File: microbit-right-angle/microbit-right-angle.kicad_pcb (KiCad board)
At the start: 2 copper layers, 58.9 x 24.4 mm, 2 parts, among them J1 microbit_edge, J2 microbit_smd_socket

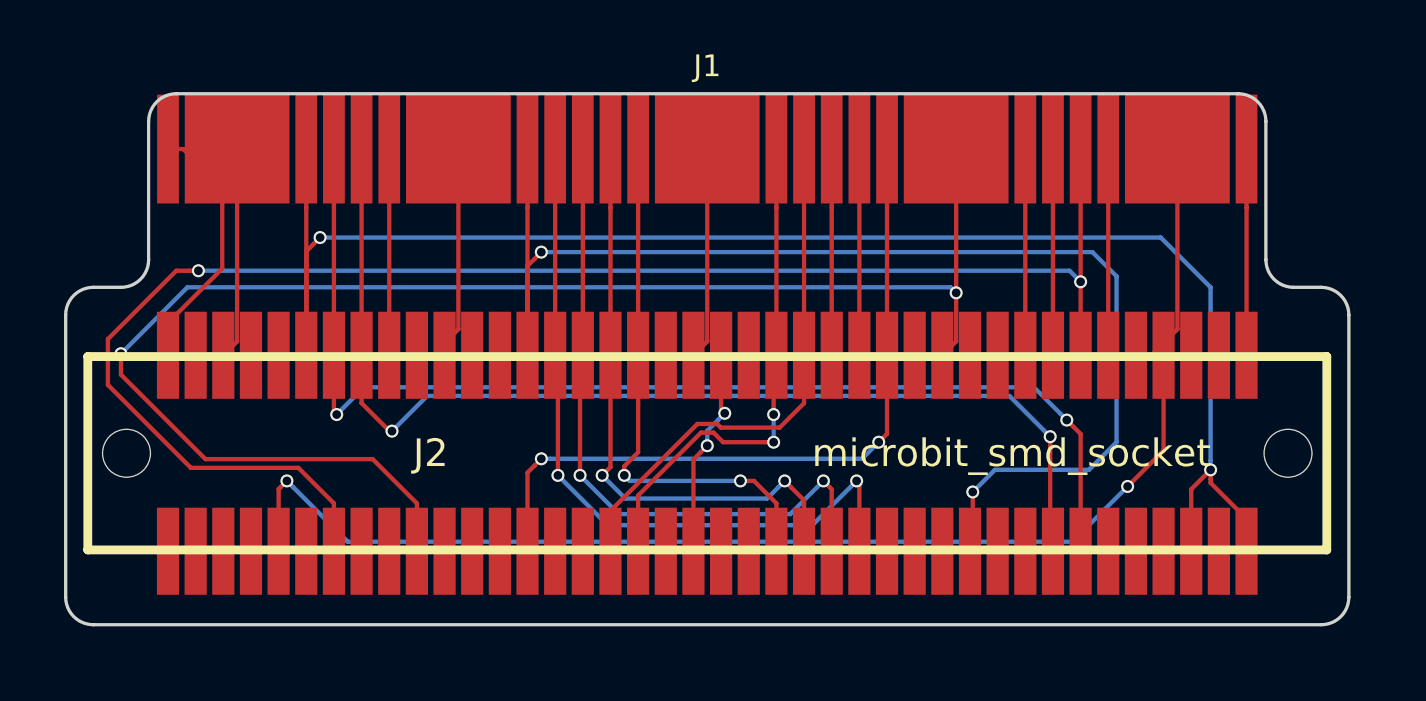
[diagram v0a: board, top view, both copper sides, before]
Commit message: Add ncss/oshw logos and URL
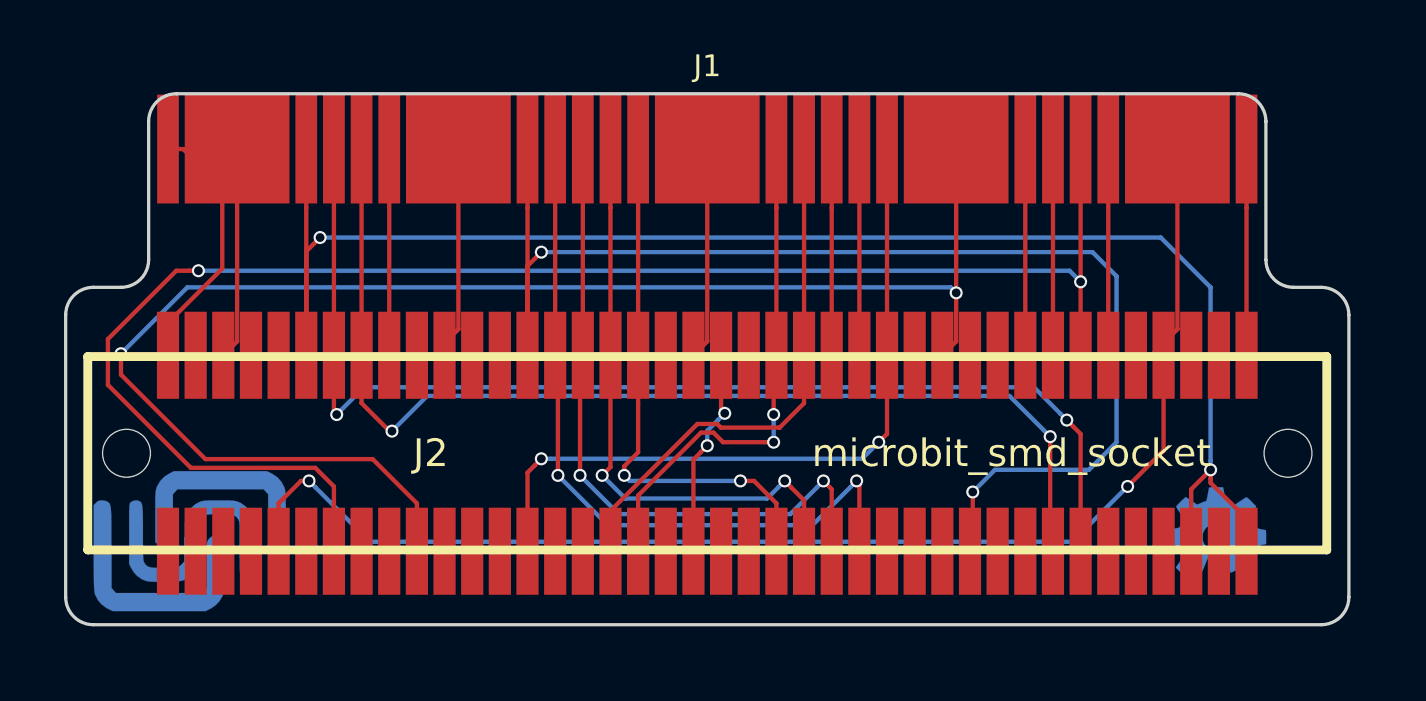
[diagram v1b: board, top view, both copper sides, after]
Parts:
- added Z1: ncss, logos:ncss, B.Cu at (127.3, 108.2)
- added Z2: oshw, logos:OSHW-Logo2_7.3x6mm_Copper, B.Cu at (174.2, 108.2)
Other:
- board text added: "github.com/jimmo/microbit-boards"

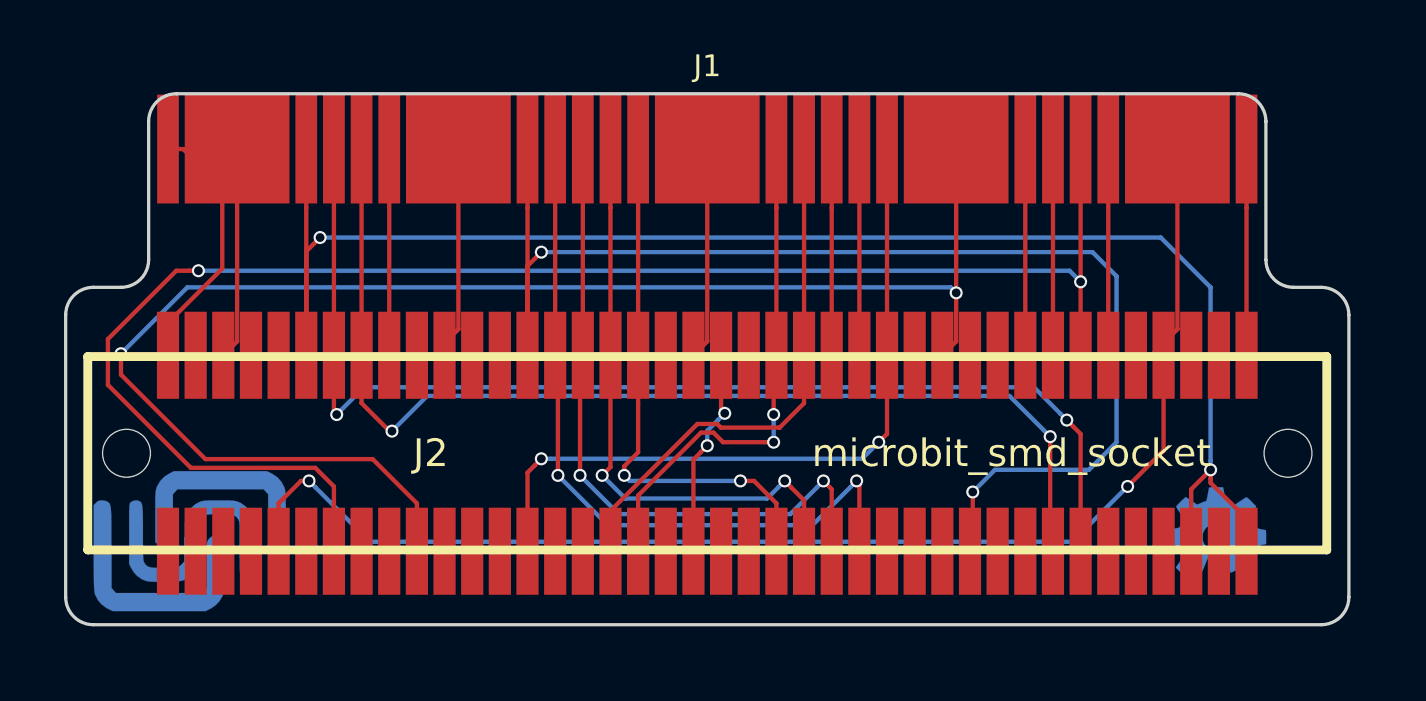
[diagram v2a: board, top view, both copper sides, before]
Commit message: Update soldermask clearance. Redo big pad connections.
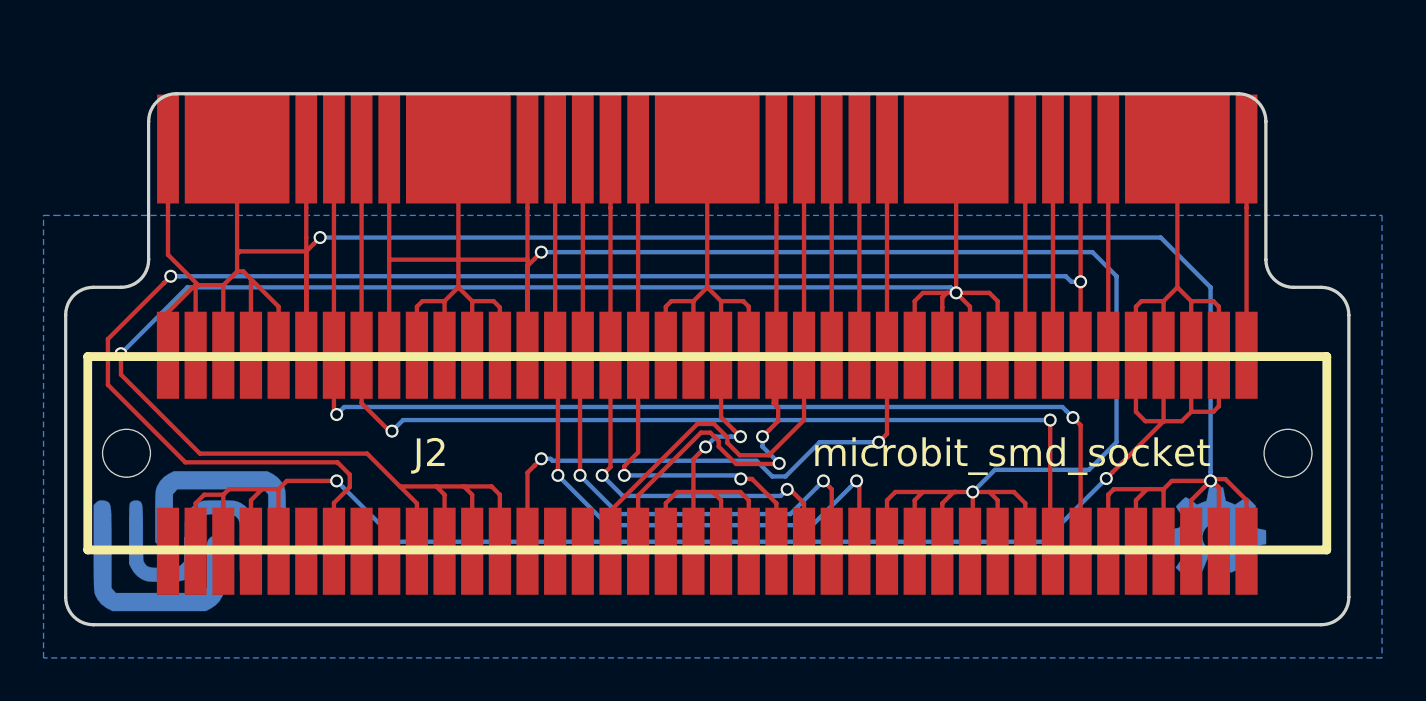
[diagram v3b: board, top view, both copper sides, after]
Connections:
- J2 pad 29: MB_3 -> (no net)
- J2 pad 30: MB_4 -> (no net)
- J2 pad 32: MB_6 -> (no net)
- J2 pad 33: MB_7 -> (no net)
- J2 pad 35: MB_9 -> (no net)
- J2 pad 36: MB_10 -> (no net)
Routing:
- net MB_0: track 68.8 -> 94.9 mm
- net MB_3V3: track 92.7 -> 117.5 mm
- net MB_GND: track 108.3 -> 128.7 mm
- net MB_2: track 27.0 -> 46.7 mm
- net MB_1: track 76.3 -> 94.7 mm
- net MB_12: track 23.7 -> 28.5 mm
- net MB_11: track 24.6 -> 26.3 mm
- net MB_5: track 73.0 -> 74.2 mm
- net MB_8: track 33.9 -> 34.6 mm
- net MB_20: track 53.2 -> 52.7 mm
- net MB_14: track 27.9 -> 27.4 mm
- added copper zone on B.Cu, net MB_GND

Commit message: Use plane fills instead of gnd/vcc traces
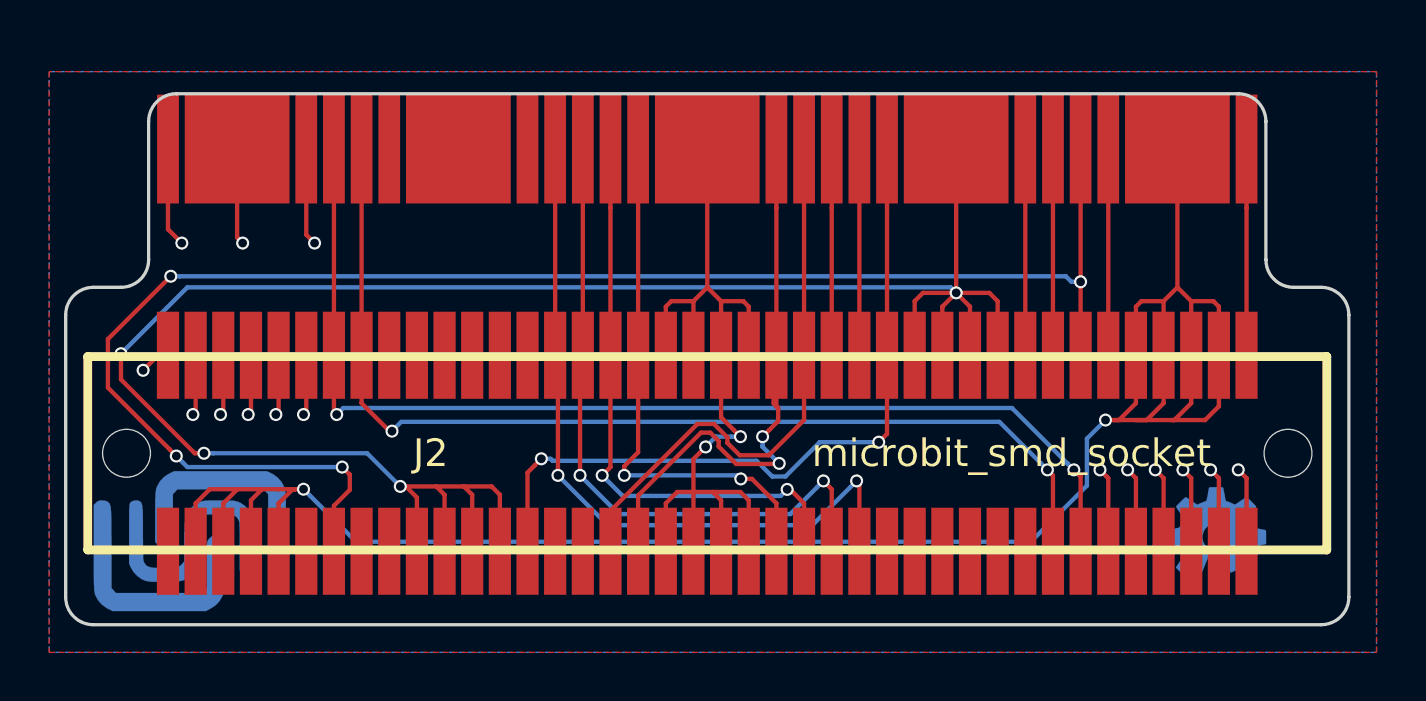
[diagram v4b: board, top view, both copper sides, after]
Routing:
- net MB_3V3: track 117.5 -> 0.00 mm, vias 2 -> 0
- net MB_GND: track 128.7 -> 52.2 mm, vias 2 -> 15
- net MB_0: track 94.9 -> 97.1 mm
- net MB_19: track 50.1 -> 48.6 mm
- net MB_20: track 52.7 -> 51.3 mm
- net MB_5: vias 2 -> 4
- net MB_1: track 94.7 -> 94.8 mm, vias 2 -> 4
- added copper zone on F.Cu, net MB_3V3

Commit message: Neaten up vias
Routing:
- net MB_8: track 34.6 -> 32.8 mm
- net MB_12: track 28.5 -> 29.6 mm
- net MB_16: track 33.8 -> 33.1 mm
- net MB_15: track 31.0 -> 30.4 mm
